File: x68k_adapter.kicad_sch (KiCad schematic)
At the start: 9 parts, among them J1 USB_A, J2 USB_A, J3 Conn_01x04, U1 PGA2040, U2 USB2422

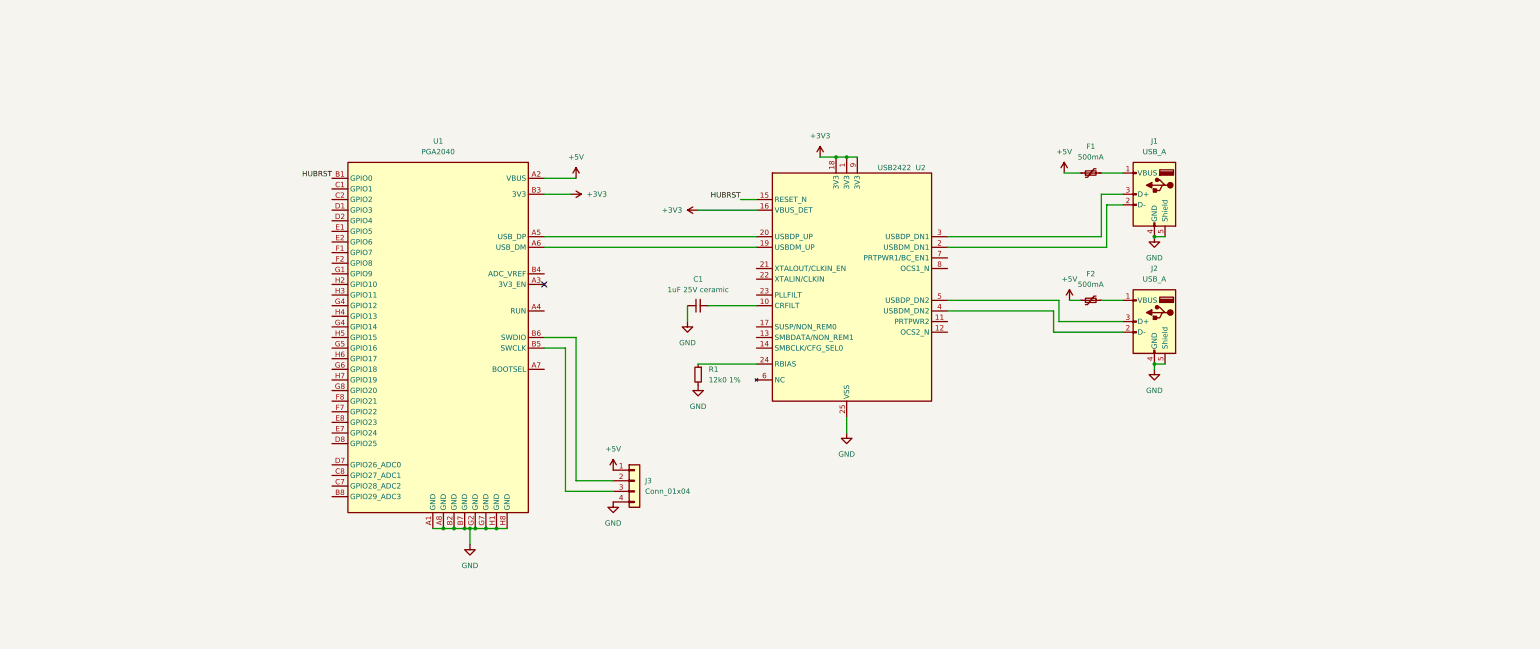
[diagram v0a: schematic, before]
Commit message: ERC passes now
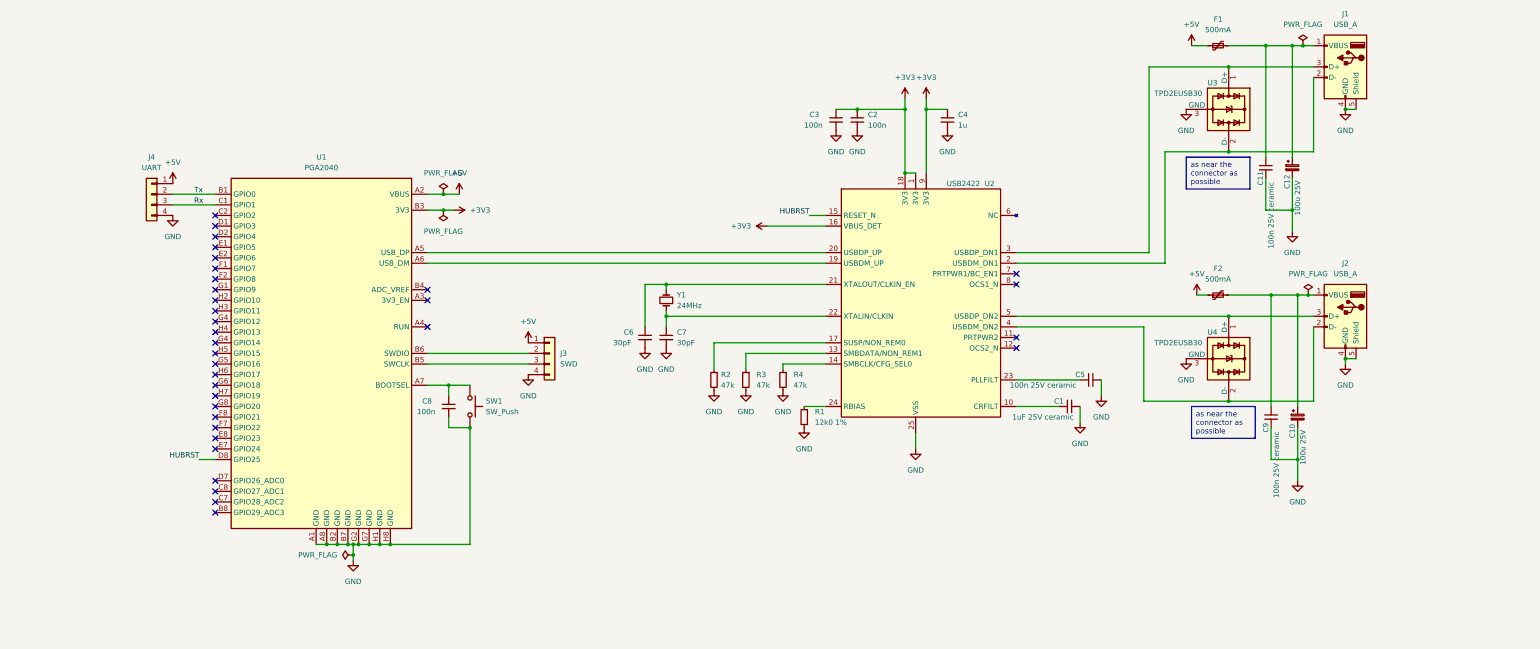
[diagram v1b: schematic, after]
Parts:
- added C10, C12: 100u 25V, symbol Device:C_Polarized_Small
- added C11, C5, C9: 100n 25V ceramic, symbol Device:C_Small
- added C2, C3, C8: 100n, symbol Device:C_Small
- added C4: 1u, symbol Device:C_Small
- added C6, C7: 30pF, symbol Device:C_Small
- added J4: UART, symbol Connector_Generic:Conn_01x04
- added R2, R3, R4: 47k, symbol Device:R_Small
- added SW1: SW_Push, symbol Switch:SW_Push
- added U3, U4: TPD2EUSB30, Package_TO_SOT_SMD:Texas_DRT-3, symbol Power_Protection:TPD2EUSB30
- added Y1: 24MHz, symbol Device:Crystal_Small
- J3: value Conn_01x04 -> SWD
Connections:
- net +3V3: now also C2.1, C3.1, C4.1
- net +5V: now also J4.1 (Pin_1)
- net GND: now also C10.2, C11.2, C12.2, C2.2, C3.2, C4.2, C5.1, C6.2, C7.2, C8.2, C9.2, J4.4 (Pin_4), R2.2, R3.2, R4.2, SW1.2, U3.3 (GND), U4.3 (GND)
- net HUBRST: now also U1.D8 (GPIO25); no longer U1.B1 (GPIO0)
- net at F2.2, J2.1 (VBUS): now also C10.1, C9.1
- net at J2.2 (D-), U2.4 (USBDM_DN2): now also U4.2 (D-)
- net at J2.3 (D+), U2.5 (USBDP_DN2): now also U4.1 (D+)
- net at U1.A7 (BOOTSEL): now also C8.1, SW1.1
- net Rx: now reaches U1.C1 (GPIO1)
- net Rx: now also J4.3 (Pin_3)
- net at U2.13 (SMBDATA/NON_REM1): now also R3.1
- net at U2.14 (SMBCLK/CFG_SEL0): now also R4.1
- net at U2.17 (SUSP/NON_REM0): now also R2.1
- net at J1.2 (D-), U2.2 (USBDM_DN1): now also U3.2 (D-)
- net at U2.21 (XTALOUT/CLKIN_EN): now also C6.1, Y1.2
- net at U2.22 (XTALIN/CLKIN): now also C7.1, Y1.1
- net at U2.23 (PLLFILT): now also C5.2
- net at J1.3 (D+), U2.3 (USBDP_DN1): now also U3.1 (D+)
- net at F1.2, J1.1 (VBUS): now also C11.1, C12.1
- new net Tx: J4.2 (Pin_2), U1.B1 (GPIO0)
- no-connect marks 1 -> 34
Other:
- title: (none) -> X2468 USB adapter for Sharp X68000
- moved on the sheet: C1, F1, F2, J1, J2, J3, R1, U1, U2

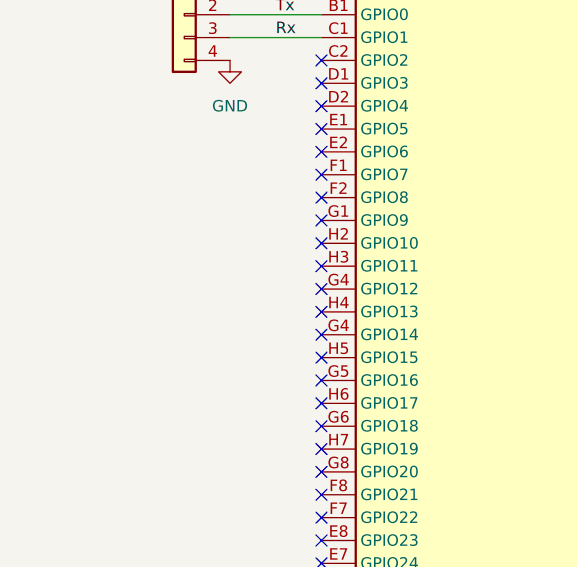
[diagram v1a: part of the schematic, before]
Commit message: Assign footprints
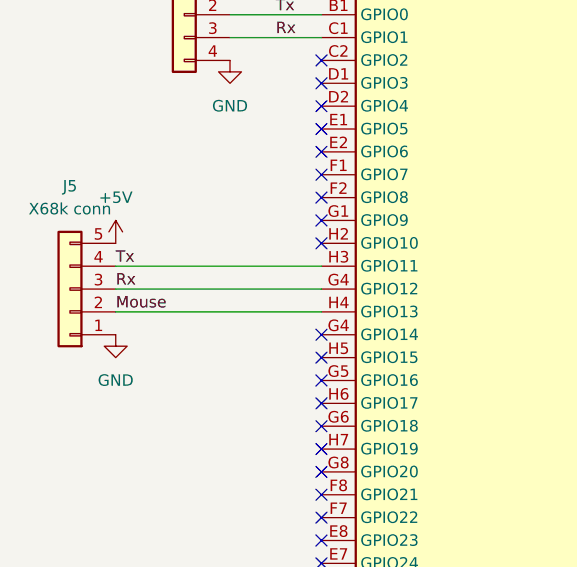
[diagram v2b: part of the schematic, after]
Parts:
- added J5: X68k conn, Connector_PinHeader_2.54mm:PinHeader_1x05_P2.54mm_Vertical, symbol Connector_Generic:Conn_01x05
- C1, C11, C5: footprint (none) -> Capacitor_THT:C_Disc_D7.5mm_W2.5mm_P5.00mm
- C10, C12: footprint (none) -> Capacitor_THT:CP_Radial_D8.0mm_P5.00mm
- C2, C3, C4, C6, C7, C8, C9: footprint (none) -> Capacitor_SMD:C_1206_3216Metric_Pad1.33x1.80mm_HandSolder
- F1, F2: footprint (none) -> Fuse:Fuse_1206_3216Metric_Pad1.42x1.75mm_HandSolder
- J1, J2: footprint (none) -> Connector_USB:USB_A_Molex_67643_Horizontal
- J3, J4: footprint (none) -> Connector_PinHeader_2.54mm:PinHeader_1x04_P2.54mm_Vertical
- R1, R2, R3, R4: footprint (none) -> Resistor_THT:R_Axial_DIN0204_L3.6mm_D1.6mm_P7.62mm_Horizontal
- SW1: footprint (none) -> Button_Switch_THT:SW_PUSH_6mm
- U2: footprint (none) -> Package_DFN_QFN:QFN-24-1EP_4x4mm_P0.5mm_EP2.6x2.6mm
- Y1: footprint (none) -> Crystal:Crystal_HC49-4H_Vertical
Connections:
- net +5V: now also J5.5 (Pin_5)
- net GND: now also J5.1 (Pin_1)
- net Rx: now also U1.G4 (GPIO14), J5.3 (Pin_3)
- net Tx: now also U1.H3 (GPIO11), J5.4 (Pin_4)
- net Mouse: now reaches U1.H4 (GPIO13)
- net Mouse: now also J5.2 (Pin_2)
- no-connect marks 34 -> 31

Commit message: route strap resistors
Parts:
- C1, C11, C5: footprint Capacitor_THT:C_Disc_D7.5mm_W2.5mm_P5.00mm -> Capacitor_THT:C_Disc_D4.3mm_W1.9mm_P5.00mm
- C10, C12: footprint Capacitor_THT:CP_Radial_D8.0mm_P5.00mm -> Capacitor_THT:CP_Radial_D4.0mm_P2.00mm
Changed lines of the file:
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@@
       (effects (font (size 1.27 1.27)) (justify left))
     )
-    (property "Footprint" "Capacitor_THT:CP_Radial_D8.0mm_P5.00mm" (at 334.01 125.73 0)
+    (property "Footprint" "Capacitor_THT:CP_Radial_D4.0mm_P2.00mm" (at 334.01 125.73 0)
       (effects (font (size 1.27 1.27)) hide)
     )
@@
       (effects (font (size 1.27 1.27)))
     )
-    (property "Footprint" "Capacitor_THT:C_Disc_D7.5mm_W2.5mm_P5.00mm" (at 326.39 66.04 0)
+    (property "Footprint" "Capacitor_THT:C_Disc_D4.3mm_W1.9mm_P5.00mm" (at 326.39 66.04 0)
       (effects (font (size 1.27 1.27)) hide)
     )
@@
       (effects (font (size 1.27 1.27)))
     )
-    (property "Footprint" "Capacitor_THT:C_Disc_D7.5mm_W2.5mm_P5.00mm" (at 279.4 123.19 0)
+    (property "Footprint" "Capacitor_THT:C_Disc_D4.3mm_W1.9mm_P5.00mm" (at 279.4 123.19 0)
       (effects (font (size 1.27 1.27)) hide)
     )
@@
       (effects (font (size 1.27 1.27)))
     )
-    (property "Footprint" "Capacitor_THT:C_Disc_D7.5mm_W2.5mm_P5.00mm" (at 284.48 116.84 0)
+    (property "Footprint" "Capacitor_THT:C_Disc_D4.3mm_W1.9mm_P5.00mm" (at 284.48 116.84 0)
       (effects (font (size 1.27 1.27)) hide)
     )
@@
       (effects (font (size 1.27 1.27)) (justify left))
     )
-    (property "Footprint" "Capacitor_THT:CP_Radial_D8.0mm_P5.00mm" (at 332.74 66.04 0)
-      (effects (font (size 1.27 1.27)) hide)
-    )
+    (property "Footprint" "Capacitor_THT:CP_Radial_D4.0mm_P2.00mm" (at 332.74 66.04 0)
+      (effects (font (size 1.27 1.27)) hide)
+    )

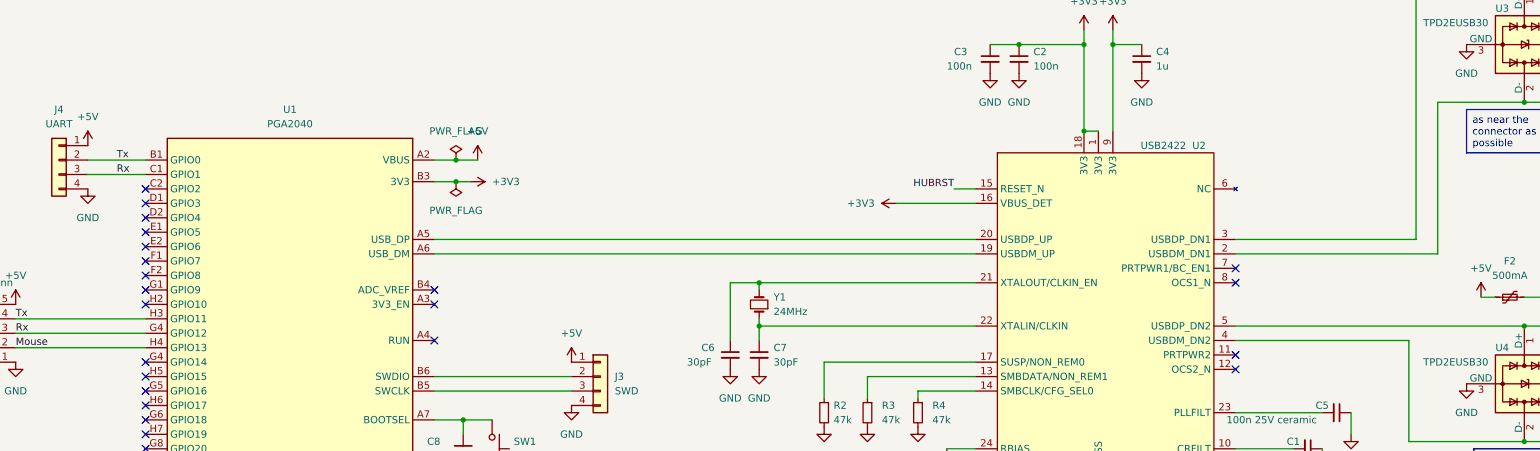
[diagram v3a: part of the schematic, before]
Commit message: General placement of the components
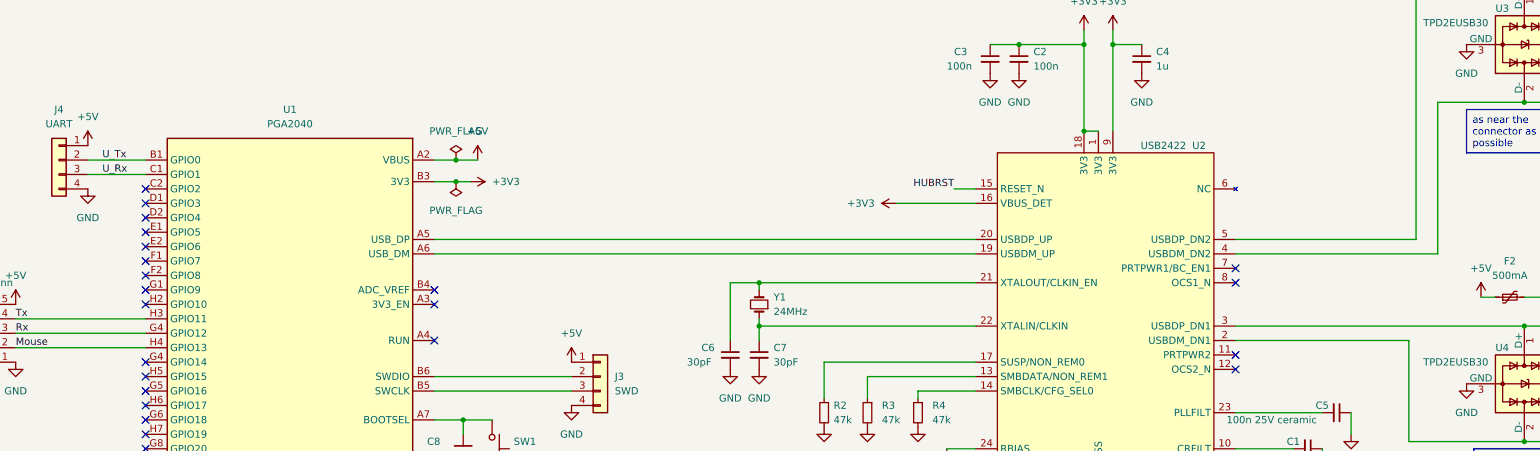
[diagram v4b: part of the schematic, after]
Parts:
- C1, C11, C5: footprint Capacitor_THT:C_Disc_D4.3mm_W1.9mm_P5.00mm -> Capacitor_SMD:C_1206_3216Metric_Pad1.33x1.80mm_HandSolder
- C10, C12: footprint Capacitor_THT:CP_Radial_D4.0mm_P2.00mm -> Capacitor_SMD:C_1206_3216Metric_Pad1.33x1.80mm_HandSolder
- R1, R2, R3, R4: footprint Resistor_THT:R_Axial_DIN0204_L3.6mm_D1.6mm_P7.62mm_Horizontal -> Resistor_SMD:R_0603_1608Metric_Pad0.98x0.95mm_HandSolder
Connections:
- net Rx: no longer J4.3 (Pin_3), U1.C1 (GPIO1)
- net Tx: no longer J4.2 (Pin_2), U1.B1 (GPIO0)
- net at J2.2 (D-), U4.2 (D-): now also U2.2 (USBDM_DN1); no longer U2.4 (USBDM_DN2)
- net at J2.3 (D+), U4.1 (D+): now also U2.3 (USBDP_DN1); no longer U2.5 (USBDP_DN2)
- net at J1.2 (D-), U3.2 (D-): now also U2.4 (USBDM_DN2); no longer U2.2 (USBDM_DN1)
- net at J1.3 (D+), U3.1 (D+): now also U2.5 (USBDP_DN2); no longer U2.3 (USBDP_DN1)
- new net U_Rx: J4.3 (Pin_3), U1.C1 (GPIO1)
- new net U_Tx: J4.2 (Pin_2), U1.B1 (GPIO0)
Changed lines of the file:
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@@
   (junction (at 107.95 158.75) (diameter 0) (color 0 0 0 0)
   )
-  (junction (at 317.5 101.6) (diameter 0) (color 0 0 0 0)
-  )
   (junction (at 107.95 156.21) (diameter 0) (color 0 0 0 0)
   )
@@
   (junction (at 130.81 118.11) (diameter 0) (color 0 0 0 0)
   )
+  (junction (at 317.5 101.6) (diameter 0) (color 0 0 0 0)
+  )
   (no_connect (at 74.93 120.65))
   (no_connect (at 74.93 85.09))
@@
     (stroke (width 0) (type default))
   )
+  (wire (pts (xy 266.7 86.36) (xy 298.45 86.36))
+    (stroke (width 0) (type default))
+  )
   (wire (pts (xy 182.88 101.6) (xy 220.98 101.6))
     (stroke (width 0) (type default))
@@
     (stroke (width 0) (type default))
   )
-  (wire (pts (xy 266.7 101.6) (xy 317.5 101.6))
-    (stroke (width 0) (type default))
-  )
   (wire (pts (xy 332.74 68.58) (xy 332.74 76.2))
     (stroke (width 0) (type default))
@@
     (stroke (width 0) (type default))
   )
+  (wire (pts (xy 266.7 101.6) (xy 317.5 101.6))
+    (stroke (width 0) (type default))
+  )
   (wire (pts (xy 326.39 68.58) (xy 326.39 76.2))
     (stroke (width 0) (type default))
@@
     (stroke (width 0) (type default))
   )
+  (wire (pts (xy 266.7 104.14) (xy 297.18 104.14))
+    (stroke (width 0) (type default))
+  )
   (wire (pts (xy 182.88 100.33) (xy 182.88 101.6))
     (stroke (width 0) (type default))
@@
     (stroke (width 0) (type default))
   )
-  (wire (pts (xy 266.7 86.36) (xy 298.45 86.36))
-    (stroke (width 0) (type default))
-  )
   (wire (pts (xy 297.18 121.92) (xy 317.5 121.92))
     (stroke (width 0) (type default))
@@
     (stroke (width 0) (type default))
   )
-  (wire (pts (xy 302.26 88.9) (xy 302.26 62.23))
+  (wire (pts (xy 302.26 62.23) (xy 302.26 88.9))
     (stroke (width 0) (type default))
   )
@@
     (stroke (width 0) (type default))
   )
-  (wire (pts (xy 266.7 104.14) (xy 297.18 104.14))
-    (stroke (width 0) (type default))
-  )
   (wire (pts (xy 317.5 101.6) (xy 337.82 101.6))
     (stroke (width 0) (type default))
@@
     (effects (font (size 1.27 1.27)) (justify left top))
   )
-  (label "Tx" (at 69.85 72.39 0) (fields_autoplaced)
+  (label "U_Tx" (at 67.31 72.39 0) (fields_autoplaced)
     (effects (font (size 1.27 1.27)) (justify left bottom))
   )
@@
     (effects (font (size 1.27 1.27)) (justify right bottom))
   )
-  (label "Rx" (at 69.85 74.93 0) (fields_autoplaced)
+  (label "U_Rx" (at 67.31 74.93 0) (fields_autoplaced)
     (effects (font (size 1.27 1.27)) (justify left bottom))
   )
@@
       (effects (font (size 1.27 1.27)) (justify left))
     )
-    (property "Footprint" "Capacitor_THT:CP_Radial_D4.0mm_P2.00mm" (at 334.01 125.73 0)
+    (property "Footprint" "Capacitor_SMD:C_1206_3216Metric_Pad1.33x1.80mm_HandSolder" (at 334.01 125.73 0)
       (effects (font (size 1.27 1.27)) hide)
     )
@@
       (effects (font (size 1.27 1.27)) (justify right))
     )
-    (property "Footprint" "Resistor_THT:R_Axial_DIN0204_L3.6mm_D1.6mm_P7.62mm_Horizontal" (at 194.31 116.84 0)
+    (property "Footprint" "Resistor_SMD:R_0603_1608Metric_Pad0.98x0.95mm_HandSolder" (at 194.31 116.84 0)
       (effects (font (size 1.27 1.27)) hide)
     )
@@
       (effects (font (size 1.27 1.27)))
     )
-    (property "Footprint" "Capacitor_THT:C_Disc_D4.3mm_W1.9mm_P5.00mm" (at 326.39 66.04 0)
+    (property "Footprint" "Capacitor_SMD:C_1206_3216Metric_Pad1.33x1.80mm_HandSolder" (at 326.39 66.04 0)
       (effects (font (size 1.27 1.27)) hide)
     )
@@
       (effects (font (size 1.27 1.27)))
     )
-    (property "Footprint" "Capacitor_THT:C_Disc_D4.3mm_W1.9mm_P5.00mm" (at 279.4 123.19 0)
+    (property "Footprint" "Capacitor_SMD:C_1206_3216Metric_Pad1.33x1.80mm_HandSolder" (at 279.4 123.19 0)
       (effects (font (size 1.27 1.27)) hide)
     )
@@
       (effects (font (size 1.27 1.27)) (justify right))
     )
-    (property "Footprint" "Resistor_THT:R_Axial_DIN0204_L3.6mm_D1.6mm_P7.62mm_Horizontal" (at 210.82 116.84 0)
+    (property "Footprint" "Resistor_SMD:R_0603_1608Metric_Pad0.98x0.95mm_HandSolder" (at 210.82 116.84 0)
       (effects (font (size 1.27 1.27)) hide)
     )
@@
       (effects (font (size 1.27 1.27)) (justify right))
     )
-    (property "Footprint" "Resistor_THT:R_Axial_DIN0204_L3.6mm_D1.6mm_P7.62mm_Horizontal" (at 215.9 125.73 0)
+    (property "Footprint" "Resistor_SMD:R_0603_1608Metric_Pad0.98x0.95mm_HandSolder" (at 215.9 125.73 0)
       (effects (font (size 1.27 1.27)) hide)
     )
@@
       (effects (font (size 1.27 1.27)))
     )
-    (property "Footprint" "Capacitor_THT:C_Disc_D4.3mm_W1.9mm_P5.00mm" (at 284.48 116.84 0)
+    (property "Footprint" "Capacitor_SMD:C_1206_3216Metric_Pad1.33x1.80mm_HandSolder" (at 284.48 116.84 0)
       (effects (font (size 1.27 1.27)) hide)
     )
@@
       (effects (font (size 1.27 1.27)) (justify left))
     )
-    (property "Footprint" "Capacitor_THT:CP_Radial_D4.0mm_P2.00mm" (at 332.74 66.04 0)
+    (property "Footprint" "Capacitor_SMD:C_1206_3216Metric_Pad1.33x1.80mm_HandSolder" (at 332.74 66.04 0)
       (effects (font (size 1.27 1.27)) hide)
     )
@@
       (effects (font (size 1.27 1.27)) (justify right))
     )
-    (property "Footprint" "Resistor_THT:R_Axial_DIN0204_L3.6mm_D1.6mm_P7.62mm_Horizontal" (at 201.93 116.84 0)
+    (property "Footprint" "Resistor_SMD:R_0603_1608Metric_Pad0.98x0.95mm_HandSolder" (at 201.93 116.84 0)
       (effects (font (size 1.27 1.27)) hide)
     )
